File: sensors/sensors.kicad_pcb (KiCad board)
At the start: 4 copper layers, 73 x 56 mm, 117 parts, among them J1 GPIO, J10 DSHOT4, J11 DSHOT5, J12 DSHOT6, J13 DSHOT7, J14 DSHOT8, J2 JP_CAN, J20 CONN_RS485, J3 JP_PWM, J4 JP_ADC, J5 JP_GPS, J6 JP_RADIO, J7 DSHOT1, J8 DSHOT2, J9 DSHOT3, SW2 SW_SPDT_321, U1 SC16IS752IPW, U10 74AHCT595, U11 SP3485EN, U2 PCA9685PW, U3 ICM-42605, U4 IST8310, U5 SPA06-003, U6 74LVC1G86, U7 ADS1115IDGS, U8 MCP2515-xST, U9 MCP2562-E-MF, Y2 25M-3225, Y4 16MHz

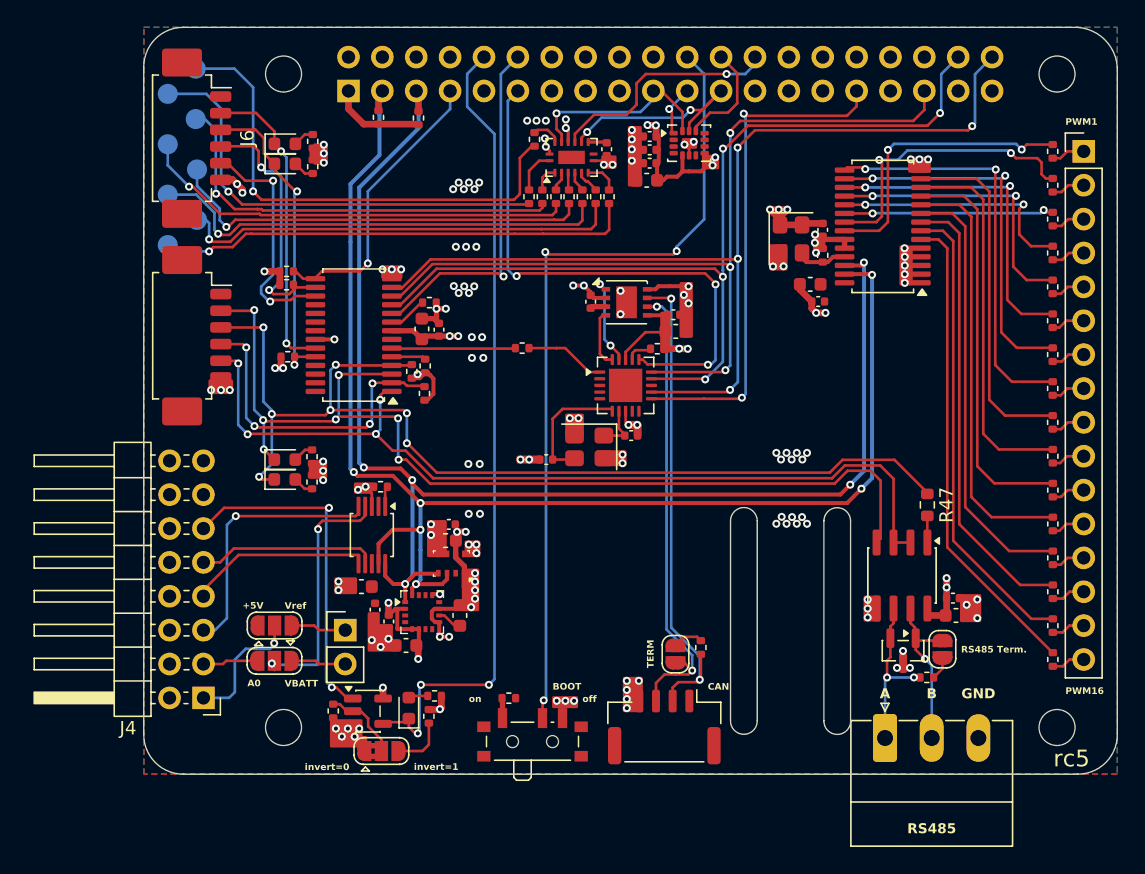
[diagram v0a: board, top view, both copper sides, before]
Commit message: fix datasheet url; layout changes
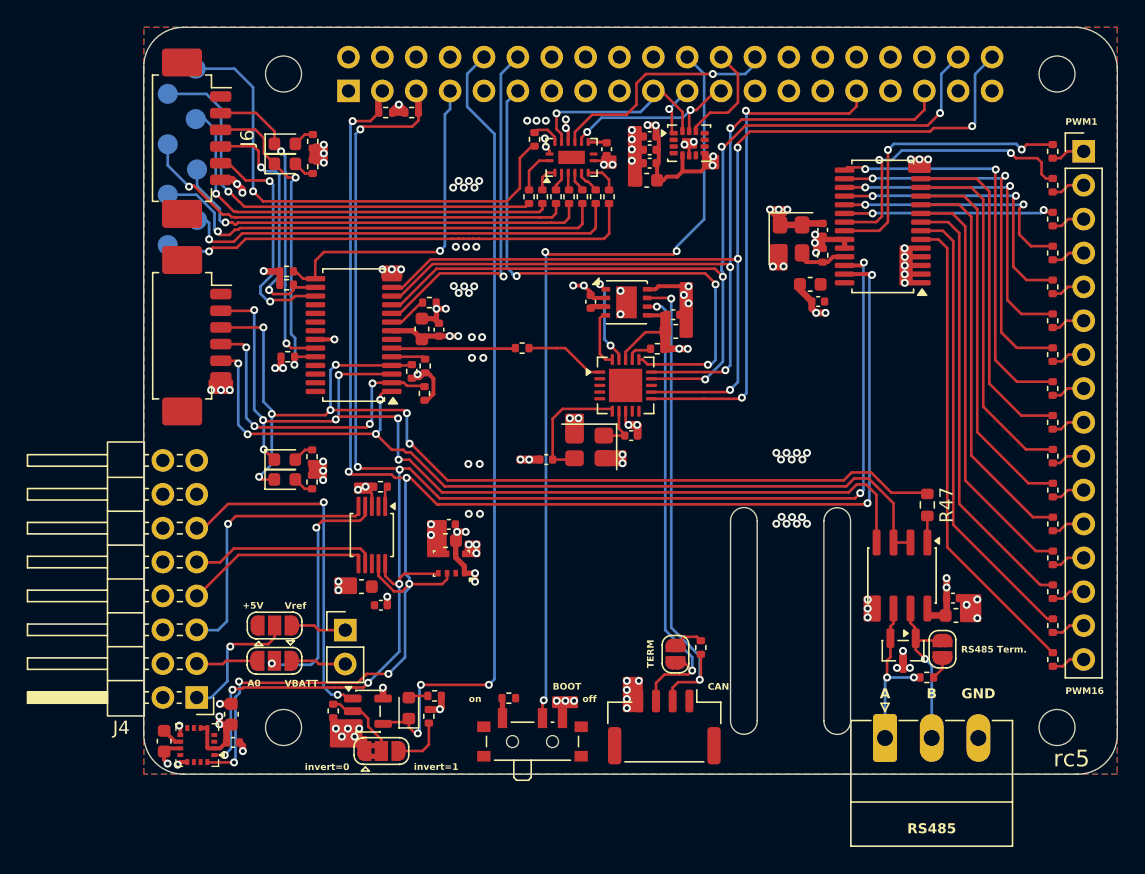
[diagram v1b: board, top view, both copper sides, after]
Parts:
- moved C10 24.1 mm to (101.5, 97.5), turned to -90 degrees
- moved U4 19.6 mm to (104.0, 97.8), turned to 180 degrees
- moved C9 14.8 mm to (106.7, 97.6), turned to 0 degrees
- moved C24 14.1 mm to (106.6, 95.5), turned to 90 degrees
- moved R34 0.65 mm to (120.1, 50.4), turned to 0 degrees
- moved R33 0.65 mm to (118.1, 50.4), turned to 180 degrees
- moved C12 0.55 mm to (117.8, 87.3), turned to 0 degrees
- moved J4 0.51 mm to (104.0, 94.3)
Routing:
- net /GPIO2/SDA1: track 103.6 -> 132.1 mm, vias 6 -> 9
- net /GPIO3/SCL1: track 102.9 -> 129.0 mm, vias 5 -> 9
- net +3V3: track 65.6 -> 58.8 mm, vias 33 -> 34
- net /GPIO4/GPCLK0: track 21.8 -> 25.1 mm
- net /GPIO11/SPI0.SCLK: track 16.2 -> 13.9 mm
- net /UART_RTSA: track 67.7 -> 65.8 mm
- net Net-(U2-LED4): track 31.9 -> 30.1 mm
- net /UART_TXA: track 77.7 -> 76.0 mm
- net GND: track 41.2 -> 39.5 mm, vias 89 -> 86
- net Net-(U2-LED5): track 30.1 -> 28.6 mm
- net /GPIO10/SPI0.MOSI: track 14.9 -> 13.7 mm
- net Net-(U2-LED6): track 28.3 -> 27.1 mm
- net Net-(U2-LED3): track 32.7 -> 31.5 mm
- net Net-(U2-LED2): track 33.9 -> 33.1 mm
- net /A0_OUT: track 19.1 -> 18.3 mm
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
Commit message: more silkscreen doc
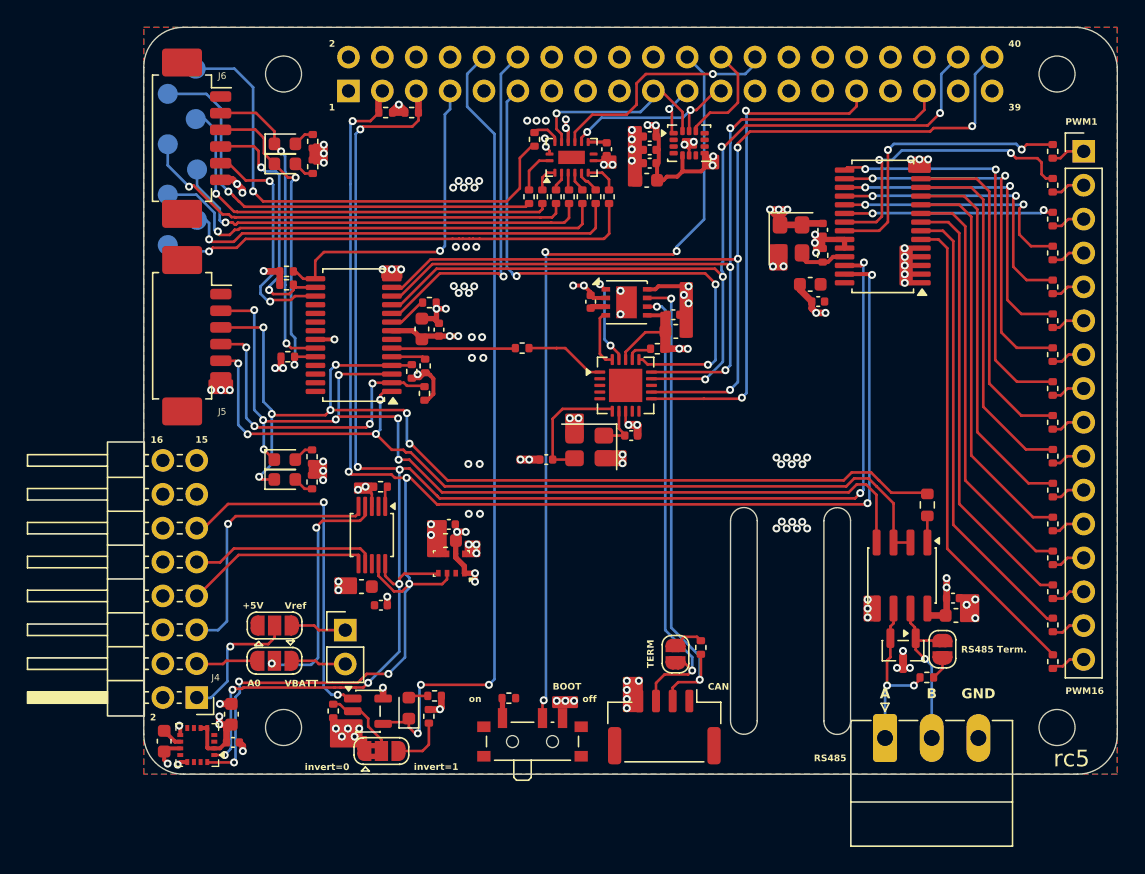
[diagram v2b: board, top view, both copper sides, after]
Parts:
- moved R28 0.16 mm to (168.2, 91.6)
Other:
- board text added: "1"
- board text added: "15"
- board text added: "16"
- board text added: "2"
- board text added: "39"
- board text added: "40"

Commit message: replace magnetometer IST8310 -> MMC5983MA
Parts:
- removed U4: IST8310, Package_LGA:LGA-16_3x3mm_P0.5mm
- added U12: MMC5983MA, Package_LGA:LGA-16_3x3mm_P0.5mm, F.Cu at (148.3, 96.1)
- C10: value 470nF 10% 25V -> 22uF 20% 10V; footprint Capacitor_SMD:C_0603_1608Metric -> Capacitor_SMD:C_0805_2012Metric
- moved C10 46.7 mm to (148.2, 98.9), turned to 0 degrees
- moved C24 41.9 mm to (148.4, 92.8)
- moved C9 40.7 mm to (147.2, 93.5), turned to 90 degrees
- moved R47 0.40 mm to (158.4, 79.8)
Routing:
- net /GPIO3/SCL1: track 129.0 -> 147.3 mm
- net /GPIO2/SDA1: track 132.1 -> 149.4 mm
- net +3V3: track 58.8 -> 65.0 mm, vias 34 -> 33
- net +5V: track 3.83 -> 9.12 mm, vias 41 -> 33
- net GND: track 39.5 -> 35.2 mm, vias 86 -> 88
- added copper zone on B.Cu, net GND
- added copper zone on F.Cu, net GND

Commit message: fix 5V on GPIO
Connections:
- R35 pad 2: +5V -> +3V3
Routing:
- net +3V3: track 65.0 -> 66.0 mm, vias 33 -> 34
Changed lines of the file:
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@@
 			(layers "F.Cu" "F.Mask" "F.Paste")
 			(roundrect_rratio 0.25)
-			(net "+5V")
+			(net "+3V3")
 			(pintype "passive")
 		)
@@
 	)
 	(segment
+		(start 127.885 95.235)
+		(end 127.9 95.25)
+		(width 0.2)
+		(layer "F.Cu")
+		(net "+3V3")
+	)
+	(segment
 		(start 149.566132 96.86675)
 		(end 150 96.86675)
@@
 	)
 	(segment
+		(start 127.885 94.3)
+		(end 127.885 95.235)
+		(width 0.4)
+		(layer "F.Cu")
+		(net "+3V3")
+	)
+	(segment
 		(start 147.710316 58.212898)
 		(end 147.710316 58.812897)
@@
 		(size 0.6)
 		(drill 0.3)
+		(layers "F.Cu" "B.Cu")
+		(net "+3V3")
+	)
+	(via
+		(at 127.9 95.25)
+		(size 0.6)
+		(drill 0.3)

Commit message: change ADC power supply to 3V3
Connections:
- C12 pad 1: +5V -> +3V3
- C26 pad 1: +5V -> +3V3
- U7 pad 8: +5V -> +3V3
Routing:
- net +3V3: track 66.0 -> 70.9 mm, vias 34 -> 36
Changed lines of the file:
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@@
 			(layers "F.Cu" "F.Mask" "F.Paste")
 			(roundrect_rratio 0.25)
-			(net "+5V")
+			(net "+3V3")
 			(pintype "passive")
 		)
@@
 			(layers "F.Cu" "F.Mask" "F.Paste")
 			(roundrect_rratio 0.25)
-			(net "+5V")
+			(net "+3V3")
 			(pintype "passive")
 		)
@@
 			(layers "F.Cu" "F.Mask" "F.Paste")
 			(roundrect_rratio 0.25)
-			(net "+5V")
+			(net "+3V3")
 			(pinfunction "VDD_8")
 			(pintype "power_in")
@@
 	)
 	(segment
+		(start 117.35 88.25)
+		(end 117.35 89)
+		(width 0.3)
+		(layer "F.Cu")
+		(net "+3V3")
+	)
+	(segment
 		(start 122.317571 94.130703)
 		(end 122.317571 95.020703)
@@
 	)
 	(segment
+		(start 117.35 88.25)
+		(end 117.35 87.380861)
+		(width 0.3)
+		(layer "F.Cu")
+		(net "+3V3")
+	)
+	(segment
 		(start 110.29 69.39)
 		(end 110.45 69.55)
@@
 	)
 	(segment
+		(start 117.100691 85.935373)
+		(end 117.100691 87.131552)
+		(width 0.3)
+		(layer "F.Cu")
+		(net "+3V3")
+	)
+	(segment
 		(start 121.49 70.107276)
 		(end 121.72 70.337276)
@@
 	)
 	(segment
+		(start 117.103193 85.932871)
+		(end 117.100691 85.935373)
+		(width 0.3)
+		(layer "F.Cu")
+		(net "+3V3")
+	)
+	(segment
 		(start 122.187571 95.150703)
 		(end 122.207571 95.130703)
@@
 	)
 	(segment
+		(start 117.100691 87.131552)
+		(end 117.302504 87.333365)
+		(width 0.3)
+		(layer "F.Cu")
+		(net "+3V3")
+	)
+	(segment
 		(start 137.748658 65.593209)
 		(end 139.19414 65.593209)
@@
 	)
 	(segment
+		(start 117.35 87.380861)
+		(end 117.302504 87.333365)
+		(width 0.3)
+		(layer "F.Cu")
+		(net "+3V3")
+	)
+	(segment
 		(start 140.01 55.195)
 		(end 140.395 54.81)
@@
 	)
 	(segment
+		(start 117.103193 84.217902)
+		(end 117.103193 85.932871)
+		(width 0.3)
+		(layer "F.Cu")
+		(net "+3V3")
+	)
+	(segment
 		(start 140.152615 68.095433)
 		(end 139.024567 68.095433)
@@
 	)
 	(via
+		(at 117.35 88.25)
+		(size 0.6)
+		(drill 0.3)
+		(layers "F.Cu" "B.Cu")
+		(net "+3V3")
+	)
+	(via
 		(at 150.1 96.96675)
 		(size 0.6)
@@
 		(size 0.6)
 		(drill 0.3)
+		(layers "F.Cu" "B.Cu")
+		(net "+3V3")
+	)
+	(via
+		(at 117.35 89)
+		(size 0.6)
+		(drill 0.3)

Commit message: use 3V3 to power PCA9685
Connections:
- C20 pad 1: +5V -> +3V3
- C4 pad 1: +5V -> +3V3
- U2 pad 28: +5V -> +3V3
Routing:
- net /GPIO2/SDA1: track 149.4 -> 124.1 mm, vias 9 -> 7
- net /GPIO3/SCL1: track 147.3 -> 123.3 mm, vias 9 -> 7
- net +3V3: track 70.9 -> 75.6 mm, vias 36 -> 38
